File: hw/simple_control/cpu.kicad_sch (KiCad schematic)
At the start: 12 parts, among them J601 Conn_01x04, J602 Raspberry_Pi_0_2_3, J603 Conn_01x03, SW601 SW_Push, U601 PicoW

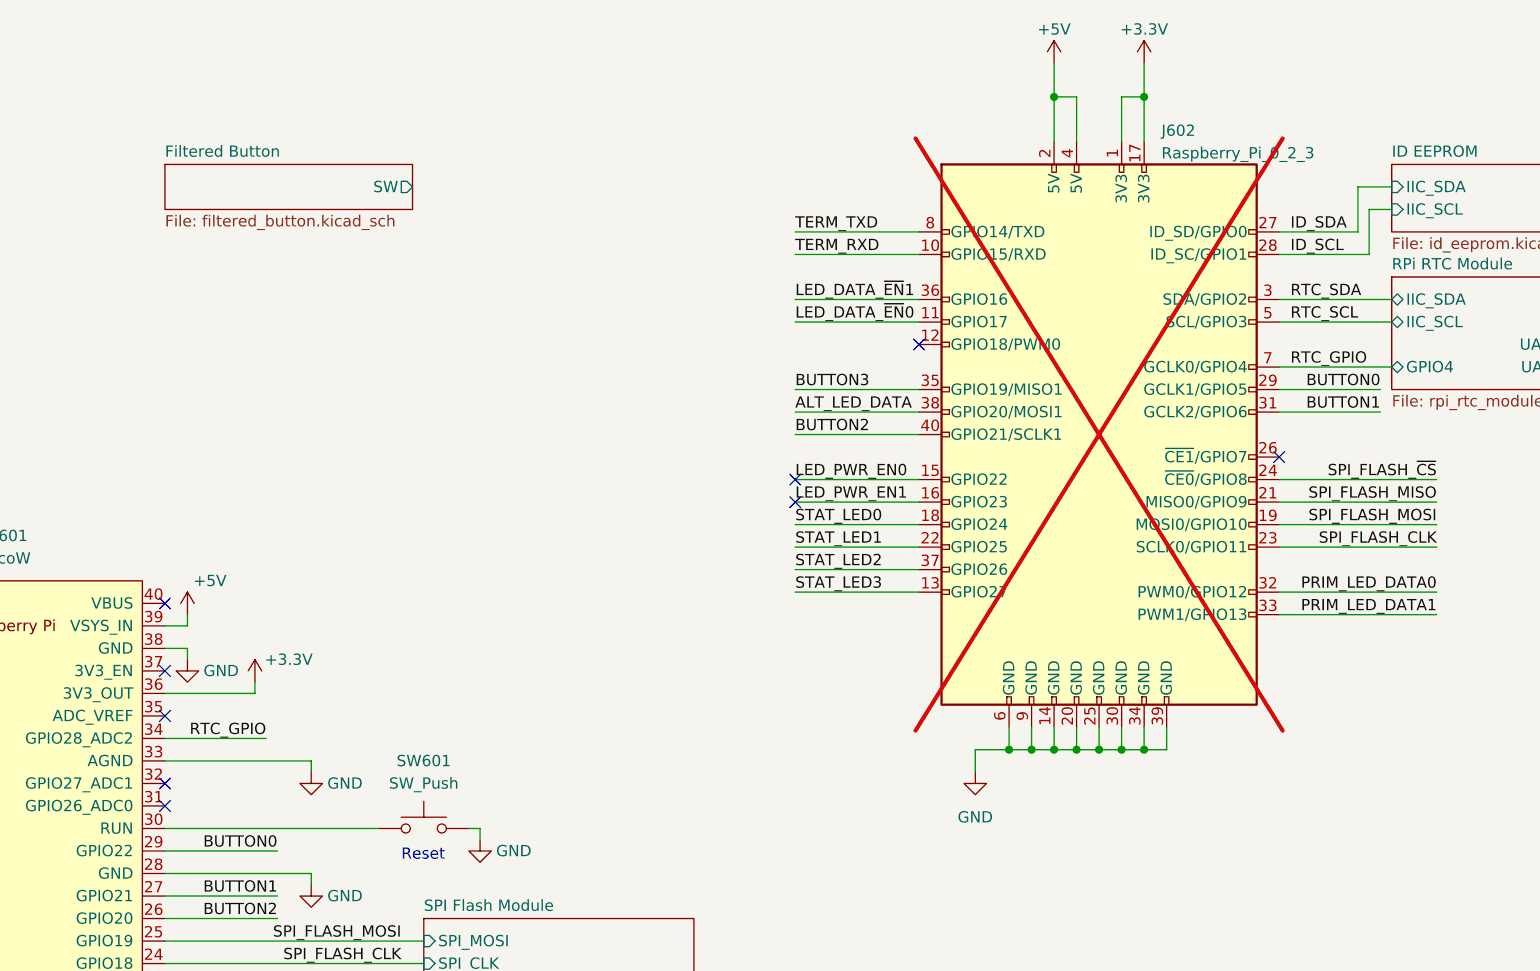
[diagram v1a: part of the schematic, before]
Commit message: chore(hw): add more buttons
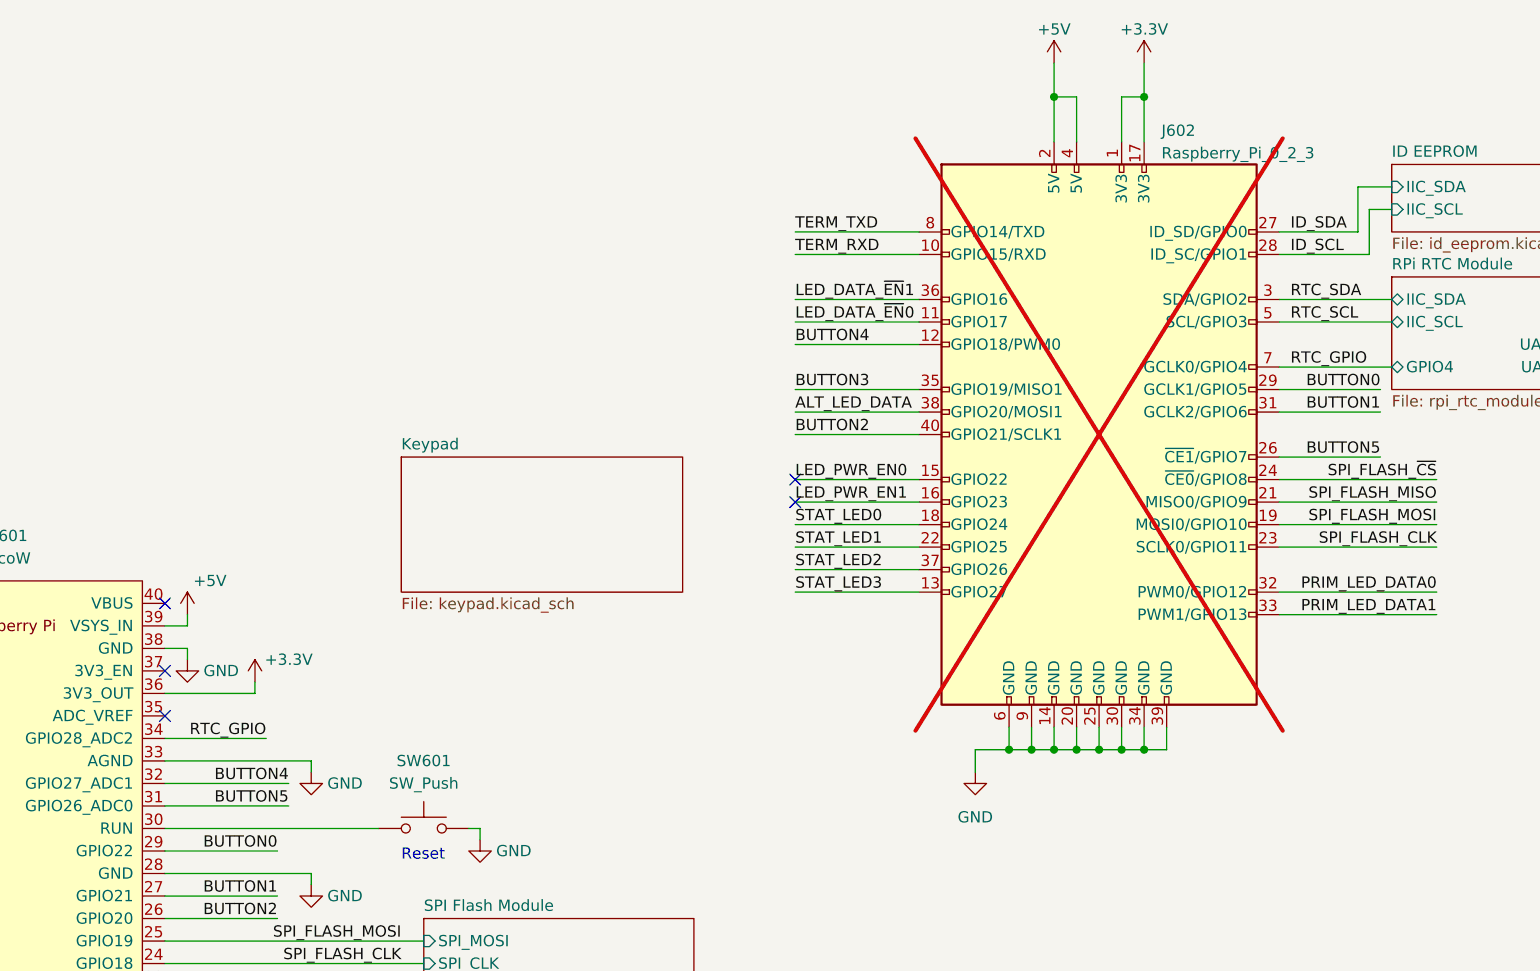
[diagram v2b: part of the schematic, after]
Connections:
- net BUTTON5: now reaches U601.31 (GPIO26_ADC0)
- net BUTTON5: now also J602.26 (~{CE1}/GPIO7)
- net BUTTON4: now reaches U601.32 (GPIO27_ADC1)
- net BUTTON4: now also J602.12 (GPIO18/PWM0)
- no-connect marks 9 -> 5
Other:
- removed sheet Filtered Button
- added sheet Keypad (keypad.kicad_sch)
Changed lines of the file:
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@@
   (junction (at 210.82 97.79) (diameter 0) (color 0 0 0 0)
   )
-  (no_connect (at 198.12 52.07))
-  (no_connect (at 113.03 104.14))
   (no_connect (at 113.03 93.98))
   (no_connect (at 113.03 88.9))
-  (no_connect (at 238.76 64.77))
-  (no_connect (at 113.03 101.6))
   (no_connect (at 113.03 81.28))
   (no_connect (at 184.15 69.85))
@@
     (stroke (width 0) (type default))
   )
+  (wire (pts (xy 113.03 104.14) (xy 127 104.14))
+    (stroke (width 0) (type default))
+  )
   (wire (pts (xy 92.71 181.61) (xy 105.41 181.61))
     (stroke (width 0) (type default))
@@
     (stroke (width 0) (type default))
   )
+  (wire (pts (xy 198.12 52.07) (xy 184.15 52.07))
+    (stroke (width 0) (type default))
+  )
   (wire (pts (xy 247.65 39.37) (xy 238.76 39.37))
     (stroke (width 0) (type default))
@@
     (stroke (width 0) (type default))
   )
+  (wire (pts (xy 238.76 64.77) (xy 250.19 64.77))
+    (stroke (width 0) (type default))
+  )
   (wire (pts (xy 114.3 129.54) (xy 114.3 133.35))
     (stroke (width 0) (type default))
@@
     (stroke (width 0) (type default))
   )
+  (wire (pts (xy 113.03 101.6) (xy 127 101.6))
+    (stroke (width 0) (type default))
+  )
   (wire (pts (xy 184.15 39.37) (xy 198.12 39.37))
     (stroke (width 0) (type default))
@@
     (effects (font (size 1.27 1.27)) (justify left bottom))
   )
+  (label "BUTTON5" (at 250.19 64.77 180) (fields_autoplaced)
+    (effects (font (size 1.27 1.27)) (justify right bottom))
+  )
   (label "BUTTON0" (at 250.19 57.15 180) (fields_autoplaced)
     (effects (font (size 1.27 1.27)) (justify right bottom))
@@
     (effects (font (size 1.27 1.27)) (justify left bottom))
   )
+  (label "BUTTON5" (at 127 104.14 180) (fields_autoplaced)
+    (effects (font (size 1.27 1.27)) (justify right bottom))
+  )
   (label "TERM_TXD" (at 281.94 50.8 90) (fields_autoplaced)
     (effects (font (size 1.27 1.27)) (justify left bottom))
@@
   )
   (label "STAT_LED0" (at 64.77 171.45 180) (fields_autoplaced)
+    (effects (font (size 1.27 1.27)) (justify right bottom))
+  )
+  (label "BUTTON4" (at 184.15 52.07 0) (fields_autoplaced)
+    (effects (font (size 1.27 1.27)) (justify left bottom))
+  )
+  (label "BUTTON4" (at 127 101.6 180) (fields_autoplaced)
     (effects (font (size 1.27 1.27)) (justify right bottom))
   )
@@
     )
   )
-  (sheet (at 113.03 31.75) (size 27.94 5.08) (fields_autoplaced)
-    (stroke (width 0.1524) (type solid))
-    (fill (color 0 0 0 0.0000))
-    (property "Sheetname" "Filtered Button" (at 113.03 31.0384 0)
-      (effects (font (size 1.27 1.27)) (justify left bottom))
-    )
-    (property "Sheetfile" "filtered_button.kicad_sch" (at 113.03 37.4146 0)
-      (effects (font (size 1.27 1.27)) (justify left top))
-    )
-    (pin "SW" output (at 140.97 34.29 0)
-      (effects (font (size 1.27 1.27)) (justify right))
-    )
-    (instances
-      (project "simple_control"
-        (path "/063164e8-0d2a-492b-8a61-e4fa4fbf06a6/3d4e7106-28aa-4335-9fa1-cc7761972854" (page "14"))
-      )
-    )
-  )
   (sheet (at 68.58 168.91) (size 24.13 5.08) (fields_autoplaced)
     (stroke (width 0.1524) (type solid))
@@
       )
     )
+  )
+  (sheet (at 139.7 64.77) (size 31.75 15.24) (fields_autoplaced)
+    (stroke (width 0.1524) (type solid))
+    (fill (color 0 0 0 0.0000))
+    (property "Sheetname" "Keypad" (at 139.7 64.0584 0)
+      (effects (font (size 1.27 1.27)) (justify left bottom))
+    )
+    (property "Sheetfile" "keypad.kicad_sch" (at 139.7 80.5946 0)
+      (effects (font (size 1.27 1.27)) (justify left top))
+    )
+    (instances
+      (project "simple_control"
+        (path "/063164e8-0d2a-492b-8a61-e4fa4fbf06a6/3d4e7106-28aa-4335-9fa1-cc7761972854" (page "15"))
+      )
+    )

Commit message: chore(hw): add buttons layout
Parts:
- renumbered SW601 to SW602
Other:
- sheet Keypad ports: added BTN0, BTN1, BTN2, BTN3; removed none
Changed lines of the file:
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@@
+    (stroke (width 0) (type default))
+  )
+  (wire (pts (xy 119.38 39.37) (xy 130.81 39.37))
     (stroke (width 0) (type default))
   )
@@
     (stroke (width 0) (type default))
   )
+  (wire (pts (xy 119.38 36.83) (xy 130.81 36.83))
+    (stroke (width 0) (type default))
+  )
   (wire (pts (xy 102.87 137.16) (xy 102.87 138.43))
     (stroke (width 0) (type default))
@@
     (stroke (width 0) (type default))
   )
+  (wire (pts (xy 119.38 34.29) (xy 130.81 34.29))
+    (stroke (width 0) (type default))
+  )
   (wire (pts (xy 135.89 185.42) (xy 135.89 187.96))
     (stroke (width 0) (type default))
@@
     (stroke (width 0) (type default))
   )
+  (wire (pts (xy 119.38 31.75) (xy 130.81 31.75))
+    (stroke (width 0) (type default))
+  )
   (wire (pts (xy 76.2 134.62) (xy 76.2 129.54))
     (stroke (width 0) (type default))
@@
     (effects (font (size 1.27 1.27)) (justify left bottom))
   )
+  (label "BUTTON3" (at 119.38 39.37 0) (fields_autoplaced)
+    (effects (font (size 1.27 1.27)) (justify left bottom))
+  )
   (label "ID_SCL" (at 240.03 41.91 0) (fields_autoplaced)
     (effects (font (size 1.27 1.27)) (justify left bottom))
@@
     (effects (font (size 1.27 1.27)) (justify right bottom))
   )
+  (label "BUTTON2" (at 119.38 36.83 0) (fields_autoplaced)
+    (effects (font (size 1.27 1.27)) (justify left bottom))
+  )
   (label "ALT_LED_DATA" (at 59.69 134.62 0) (fields_autoplaced)
     (effects (font (size 1.27 1.27)) (justify left bottom))
@@
     (effects (font (size 1.27 1.27)) (justify left bottom))
   )
+  (label "BUTTON1" (at 119.38 34.29 0) (fields_autoplaced)
+    (effects (font (size 1.27 1.27)) (justify left bottom))
+  )
   (label "PRIM_LED_DATA1" (at 59.69 119.38 0) (fields_autoplaced)
     (effects (font (size 1.27 1.27)) (justify left bottom))
@@
   )
   (label "TERM_TXD" (at 281.94 50.8 90) (fields_autoplaced)
+    (effects (font (size 1.27 1.27)) (justify left bottom))
+  )
+  (label "BUTTON0" (at 119.38 31.75 0) (fields_autoplaced)
     (effects (font (size 1.27 1.27)) (justify left bottom))
   )
@@
   (symbol (lib_id "Switch:SW_Push") (at 142.24 106.68 0) (unit 1)
     (in_bom yes) (on_board yes) (dnp no) (fields_autoplaced)
-    (property "Reference" "SW601" (at 142.24 99.06 0)
+    (property "Reference" "SW602" (at 142.24 99.06 0)
       (effects (font (size 1.27 1.27)))
     )
@@
       (project "simple_control"
         (path "/063164e8-0d2a-492b-8a61-e4fa4fbf06a6/3d4e7106-28aa-4335-9fa1-cc7761972854"
-          (reference "SW601") (unit 1)
+          (reference "SW602") (unit 1)
         )
       )
@@
     )
   )
-  (sheet (at 139.7 64.77) (size 31.75 15.24) (fields_autoplaced)
+  (sheet (at 130.81 27.94) (size 31.75 15.24) (fields_autoplaced)
     (stroke (width 0.1524) (type solid))
     (fill (color 0 0 0 0.0000))
-    (property "Sheetname" "Keypad" (at 139.7 64.0584 0)
+    (property "Sheetname" "Keypad" (at 130.81 27.2284 0)
       (effects (font (size 1.27 1.27)) (justify left bottom))
     )
-    (property "Sheetfile" "keypad.kicad_sch" (at 139.7 80.5946 0)
+    (property "Sheetfile" "keypad.kicad_sch" (at 130.81 43.7646 0)
       (effects (font (size 1.27 1.27)) (justify left top))
     )
-    (instances
+    (pin "BTN2" output (at 130.81 36.83 180)
+      (effects (font (size 1.27 1.27)) (justify left))
+    )
+    (pin "BTN3" output (at 130.81 39.37 180)
+      (effects (font (size 1.27 1.27)) (justify left))
+    )
+    (pin "BTN0" output (at 130.81 31.75 180)
+      (effects (font (size 1.27 1.27)) (justify left))
+    )
+    (pin "BTN1" output (at 130.81 34.29 180)
+      (effects (font (size 1.27 1.27)) (justify left))
+    )
+    (instances

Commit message: chore(hw): major layout update
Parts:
- removed C603: 100n, Capacitor_SMD:C_0805_2012Metric_Pad1.18x1.45mm_HandSolder, symbol Device:C
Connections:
- net BUTTON4: no longer names the net of U601.32 (GPIO27_ADC1)
- net BUTTON4: no longer J602.12 (GPIO18/PWM0)
- net BUTTON5: no longer names the net of U601.31 (GPIO26_ADC0)
- net BUTTON5: no longer J602.26 (~{CE1}/GPIO7)
- no-connect marks 5 -> 9
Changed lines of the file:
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@@
   (junction (at 223.52 24.13) (diameter 0) (color 0 0 0 0)
   )
-  (junction (at 148.59 185.42) (diameter 0) (color 0 0 0 0)
-  )
-  (junction (at 148.59 175.26) (diameter 0) (color 0 0 0 0)
-  )
   (junction (at 95.25 137.16) (diameter 0) (color 0 0 0 0)
   )
   (junction (at 210.82 97.79) (diameter 0) (color 0 0 0 0)
   )
+  (no_connect (at 113.03 104.14))
+  (no_connect (at 198.12 52.07))
   (no_connect (at 113.03 93.98))
   (no_connect (at 113.03 88.9))
+  (no_connect (at 238.76 64.77))
+  (no_connect (at 113.03 101.6))
   (no_connect (at 113.03 81.28))
   (no_connect (at 184.15 69.85))
@@
     (stroke (width 0) (type default))
   )
-  (wire (pts (xy 161.29 185.42) (xy 161.29 184.15))
-    (stroke (width 0) (type default))
-  )
   (wire (pts (xy 72.39 53.34) (xy 72.39 59.69))
     (stroke (width 0) (type default))
@@
     (stroke (width 0) (type default))
   )
-  (wire (pts (xy 113.03 104.14) (xy 127 104.14))
-    (stroke (width 0) (type default))
-  )
   (wire (pts (xy 92.71 181.61) (xy 105.41 181.61))
     (stroke (width 0) (type default))
@@
     (stroke (width 0) (type default))
   )
-  (wire (pts (xy 148.59 185.42) (xy 161.29 185.42))
-    (stroke (width 0) (type default))
-  )
   (wire (pts (xy 259.08 160.02) (xy 259.08 161.29))
     (stroke (width 0) (type default))
   )
-  (wire (pts (xy 198.12 52.07) (xy 184.15 52.07))
-    (stroke (width 0) (type default))
-  )
   (wire (pts (xy 247.65 39.37) (xy 238.76 39.37))
     (stroke (width 0) (type default))
@@
     (stroke (width 0) (type default))
   )
-  (wire (pts (xy 238.76 64.77) (xy 250.19 64.77))
-    (stroke (width 0) (type default))
-  )
   (wire (pts (xy 114.3 129.54) (xy 114.3 133.35))
     (stroke (width 0) (type default))
@@
     (stroke (width 0) (type default))
   )
-  (wire (pts (xy 148.59 175.26) (xy 161.29 175.26))
-    (stroke (width 0) (type default))
-  )
   (wire (pts (xy 184.15 69.85) (xy 198.12 69.85))
     (stroke (width 0) (type default))
@@
     (stroke (width 0) (type default))
   )
-  (wire (pts (xy 113.03 101.6) (xy 127 101.6))
-    (stroke (width 0) (type default))
-  )
   (wire (pts (xy 184.15 39.37) (xy 198.12 39.37))
     (stroke (width 0) (type default))
@@
     (stroke (width 0) (type default))
   )
-  (wire (pts (xy 161.29 175.26) (xy 161.29 176.53))
-    (stroke (width 0) (type default))
-  )
   (wire (pts (xy 198.12 57.15) (xy 184.15 57.15))
     (stroke (width 0) (type default))
@@
     (effects (font (size 1.27 1.27)) (justify left bottom))
   )
-  (label "BUTTON5" (at 250.19 64.77 180) (fields_autoplaced)
-    (effects (font (size 1.27 1.27)) (justify right bottom))
-  )
   (label "BUTTON0" (at 250.19 57.15 180) (fields_autoplaced)
     (effects (font (size 1.27 1.27)) (justify right bottom))
@@
     (effects (font (size 1.27 1.27)) (justify left bottom))
   )
-  (label "BUTTON5" (at 127 104.14 180) (fields_autoplaced)
-    (effects (font (size 1.27 1.27)) (justify right bottom))
-  )
   (label "TERM_TXD" (at 281.94 50.8 90) (fields_autoplaced)
     (effects (font (size 1.27 1.27)) (justify left bottom))
@@
   )
   (label "STAT_LED0" (at 64.77 171.45 180) (fields_autoplaced)
-    (effects (font (size 1.27 1.27)) (justify right bottom))
-  )
-  (label "BUTTON4" (at 184.15 52.07 0) (fields_autoplaced)
-    (effects (font (size 1.27 1.27)) (justify left bottom))
-  )
-  (label "BUTTON4" (at 127 101.6 180) (fields_autoplaced)
     (effects (font (size 1.27 1.27)) (justify right bottom))
   )
@@
         )
       )
-    )
-  )
-  (symbol (lib_id "Device:C") (at 161.29 180.34 0) (unit 1)
-    (in_bom no) (on_board yes) (dnp yes) (fields_autoplaced)
-    (property "Reference" "C603" (at 165.1 179.07 0)
-      (effects (font (size 1.27 1.27)) (justify left))
-    )
-    (property "Value" "100n" (at 165.1 181.61 0)
-      (effects (font (size 1.27 1.27)) (justify left))
-    )
-    (property "Footprint" "Capacitor_SMD:C_0805_2012Metric_Pad1.18x1.45mm_HandSolder" (at 162.2552 184.15 0)
-      (effects (font (size 1.27 1.27)) hide)
-    )
-    (property "Datasheet" "~" (at 161.29 180.34 0)
-      (effects (font (size 1.27 1.27)) hide)
-    )
-    (pin "1")
-    (pin "2")
-    (instances
-      (project "simple_control"
-        (path "/063164e8-0d2a-492b-8a61-e4fa4fbf06a6/3d4e7106-28aa-4335-9fa1-cc7761972854"
-          (reference "C603") (unit 1)
-        )
-      )

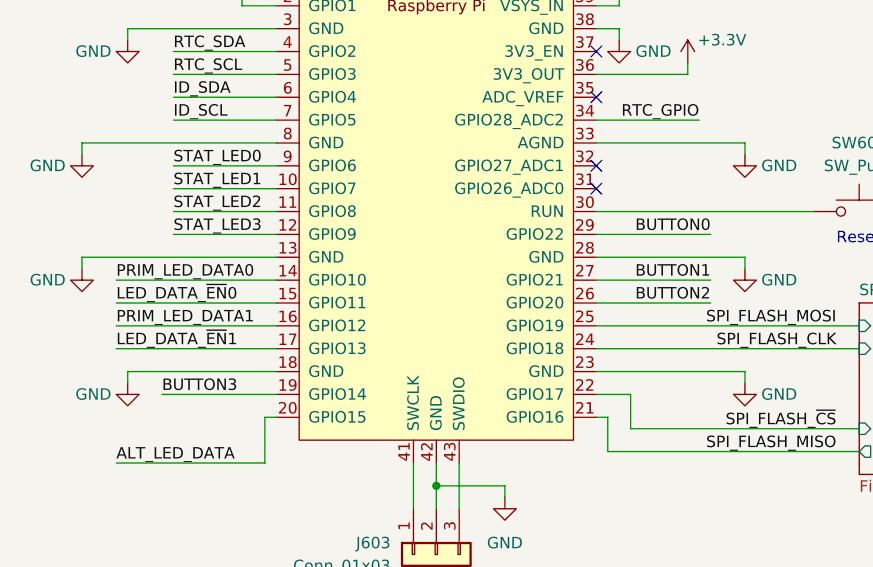
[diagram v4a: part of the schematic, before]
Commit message: chore(hw): layout LED EN and DATA
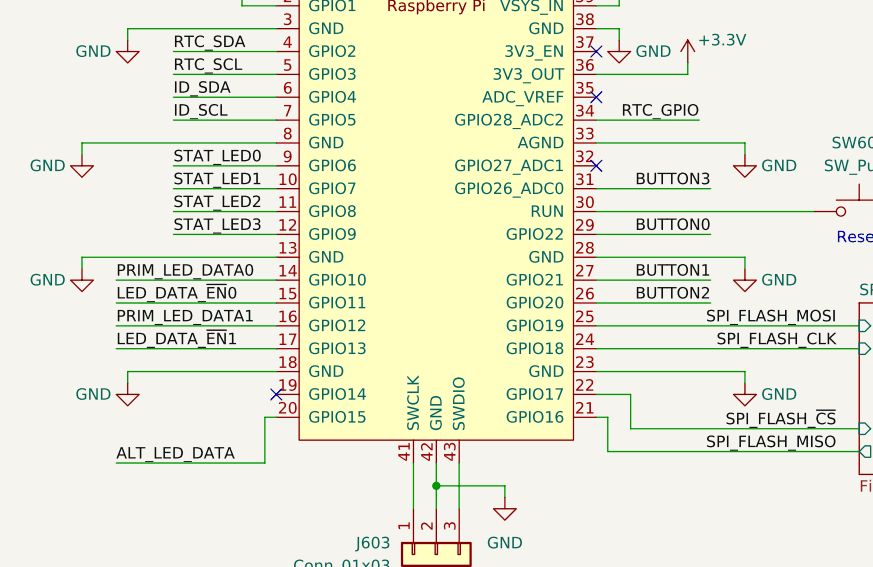
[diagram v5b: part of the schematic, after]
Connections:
- net BUTTON3: now also U601.31 (GPIO26_ADC0); no longer U601.19 (GPIO14)
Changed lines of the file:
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@@
   (junction (at 210.82 97.79) (diameter 0) (color 0 0 0 0)
   )
-  (no_connect (at 113.03 104.14))
   (no_connect (at 198.12 52.07))
   (no_connect (at 113.03 93.98))
   (no_connect (at 113.03 88.9))
+  (no_connect (at 77.47 127))
   (no_connect (at 238.76 64.77))
   (no_connect (at 113.03 101.6))
@@
     (stroke (width 0) (type default))
   )
-  (wire (pts (xy 77.47 127) (xy 64.77 127))
+  (wire (pts (xy 113.03 104.14) (xy 125.73 104.14))
     (stroke (width 0) (type default))
   )
@@
     (effects (font (size 1.27 1.27)) (justify right bottom))
   )
-  (label "BUTTON3" (at 64.77 127 0) (fields_autoplaced)
-    (effects (font (size 1.27 1.27)) (justify left bottom))
+  (label "BUTTON3" (at 125.73 104.14 180) (fields_autoplaced)
+    (effects (font (size 1.27 1.27)) (justify right bottom))
   )
   (label "BUTTON1" (at 125.73 114.3 180) (fields_autoplaced)
